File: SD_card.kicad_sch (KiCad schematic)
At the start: 1 part, among them J6 TF-15x15

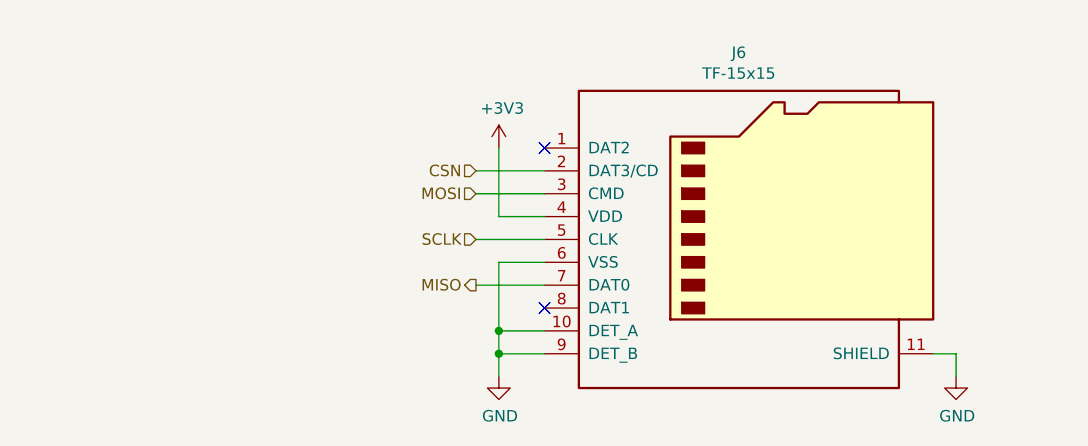
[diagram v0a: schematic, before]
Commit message: Move to KiCad v6, redesign circuit for chamber
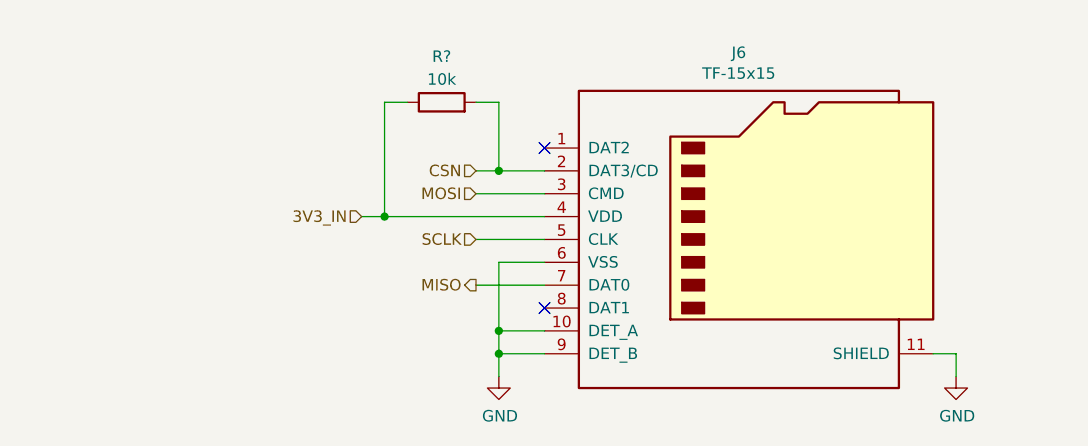
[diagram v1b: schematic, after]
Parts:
- added R?: 10k, Resistor_SMD:R_0603_1608Metric, symbol Device:R
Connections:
- net CSN: now also R?.2
- net +3V3 renamed 3V3_IN
- net 3V3_IN: now also R?.1
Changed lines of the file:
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@@
 (kicad_sch (version 20211123) (generator eeschema)
   (paper "A4")
+  (junction (at 127 91.44) (diameter 0) (color 0 0 0 0)
+  )
   (junction (at 127 109.22) (diameter 0) (color 0 0 0 0)
+  )
+  (junction (at 114.3 96.52) (diameter 0) (color 0 0 0 0)
   )
   (junction (at 127 111.76) (diameter 0) (color 0 0 0 0)
@@
   (no_connect (at 132.08 88.9))
   (no_connect (at 132.08 106.68))
+  (wire (pts (xy 114.3 96.52) (xy 132.08 96.52))
+    (stroke (width 0) (type default) (color 0 0 0 0))
+  )
+  (wire (pts (xy 127 91.44) (xy 132.08 91.44))
+    (stroke (width 0) (type default) (color 0 0 0 0))
+  )
+  (wire (pts (xy 116.84 83.82) (xy 114.3 83.82))
+    (stroke (width 0) (type default) (color 0 0 0 0))
+  )
+  (wire (pts (xy 111.76 96.52) (xy 114.3 96.52))
+    (stroke (width 0) (type default) (color 0 0 0 0))
+  )
   (wire (pts (xy 127 101.6) (xy 127 109.22))
     (stroke (width 0) (type default) (color 0 0 0 0))
   )
-  (wire (pts (xy 127 96.52) (xy 127 88.9))
+  (wire (pts (xy 127 83.82) (xy 127 91.44))
     (stroke (width 0) (type default) (color 0 0 0 0))
   )
@@
     (stroke (width 0) (type default) (color 0 0 0 0))
   )
-  (wire (pts (xy 132.08 96.52) (xy 127 96.52))
-    (stroke (width 0) (type default) (color 0 0 0 0))
-  )
   (wire (pts (xy 132.08 111.76) (xy 127 111.76))
     (stroke (width 0) (type default) (color 0 0 0 0))
   )
   (wire (pts (xy 124.46 99.06) (xy 132.08 99.06))
+    (stroke (width 0) (type default) (color 0 0 0 0))
+  )
+  (wire (pts (xy 114.3 83.82) (xy 114.3 96.52))
     (stroke (width 0) (type default) (color 0 0 0 0))
   )
@@
     (stroke (width 0) (type default) (color 0 0 0 0))
   )
-  (wire (pts (xy 124.46 91.44) (xy 132.08 91.44))
+  (wire (pts (xy 124.46 91.44) (xy 127 91.44))
     (stroke (width 0) (type default) (color 0 0 0 0))
   )
   (wire (pts (xy 127 111.76) (xy 127 114.3))
+    (stroke (width 0) (type default) (color 0 0 0 0))
+  )
+  (wire (pts (xy 127 83.82) (xy 124.46 83.82))
     (stroke (width 0) (type default) (color 0 0 0 0))
   )
@@
   )
   (hierarchical_label "MISO" (shape output) (at 124.46 104.14 180)
+    (effects (font (size 1.27 1.27)) (justify right))
+  )
+  (hierarchical_label "3V3_IN" (shape input) (at 111.76 96.52 180)
     (effects (font (size 1.27 1.27)) (justify right))
   )
@@
     )
     (property "Datasheet" "" (id 3) (at 127 114.3 0)
-      (effects (font (size 1.27 1.27)) hide)
-    )
-    (pin "1")
-  )
-  (symbol (lib_id "power:+3V3") (at 127 88.9 0) (unit 1)
-    (in_bom yes) (on_board yes)
-    (property "Reference" "#PWR013" (id 0) (at 127 92.71 0)
-      (effects (font (size 1.27 1.27)) hide)
-    )
-    (property "Value" "+3V3" (id 1) (at 127.381 84.5058 0))
-    (property "Footprint" "" (id 2) (at 127 88.9 0)
-      (effects (font (size 1.27 1.27)) hide)
-    )
-    (property "Datasheet" "" (id 3) (at 127 88.9 0)
       (effects (font (size 1.27 1.27)) hide)
     )
@@
     (pin "9")
   )
+  (symbol (lib_id "Device:R") (at 120.65 83.82 90) (unit 1)
+    (in_bom yes) (on_board yes)
+    (property "Reference" "R?" (id 0) (at 120.65 78.74 90))
+    (property "Value" "10k" (id 1) (at 120.65 81.28 90))
+    (property "Footprint" "Resistor_SMD:R_0603_1608Metric" (id 2) (at 120.65 85.598 90)
+      (effects (font (size 1.27 1.27)) hide)
+    )
+    (property "Datasheet" "~" (id 3) (at 120.65 83.82 0)
+      (effects (font (size 1.27 1.27)) hide)
+    )
+    (property "LCSC" "C25804" (id 4) (at 120.65 83.82 0)
+      (effects (font (size 1.27 1.27)) hide)
+    )
+    (pin "1")
+    (pin "2")
+  )
 )

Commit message: Add test points, add JLC part numbers to JST XH connectors, clean up
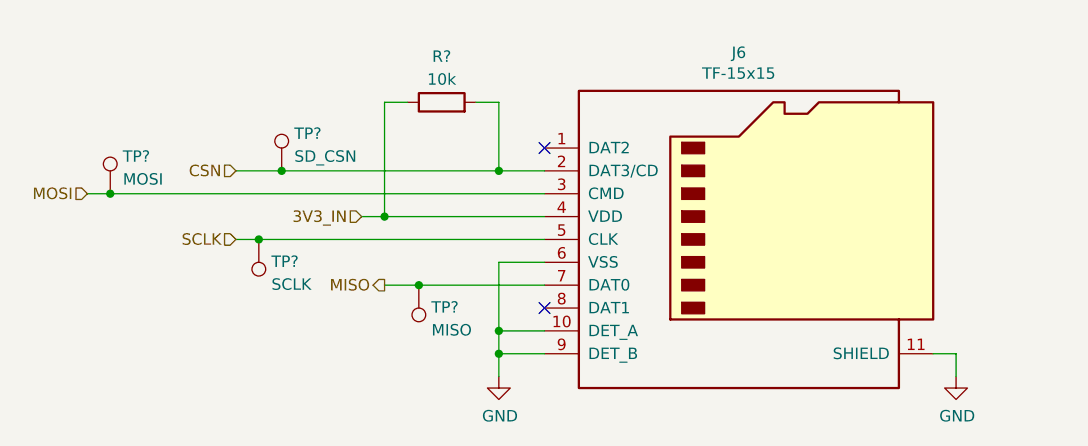
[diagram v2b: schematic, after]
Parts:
- added TP?: MOSI, symbol Connector:TestPoint
- added TP?: SD_CSN, symbol Connector:TestPoint
- added TP?: MISO, symbol Connector:TestPoint
- added TP?: SCLK, symbol Connector:TestPoint
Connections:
- net CSN: now also TP?.1
- net MISO: now also TP?.1
- net MOSI: now also TP?.1
- net SCLK: now also TP?.1
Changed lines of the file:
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@@
   (junction (at 127 109.22) (diameter 0) (color 0 0 0 0)
+  )
+  (junction (at 100.33 99.06) (diameter 0) (color 0 0 0 0)
+  )
+  (junction (at 118.11 104.14) (diameter 0) (color 0 0 0 0)
+  )
+  (junction (at 102.87 91.44) (diameter 0) (color 0 0 0 0)
+  )
+  (junction (at 83.82 93.98) (diameter 0) (color 0 0 0 0)
   )
   (junction (at 114.3 96.52) (diameter 0) (color 0 0 0 0)
@@
     (stroke (width 0) (type default) (color 0 0 0 0))
   )
+  (wire (pts (xy 100.33 99.06) (xy 132.08 99.06))
+    (stroke (width 0) (type default) (color 0 0 0 0))
+  )
   (wire (pts (xy 116.84 83.82) (xy 114.3 83.82))
     (stroke (width 0) (type default) (color 0 0 0 0))
@@
     (stroke (width 0) (type default) (color 0 0 0 0))
   )
-  (wire (pts (xy 124.46 104.14) (xy 132.08 104.14))
+  (wire (pts (xy 114.3 104.14) (xy 118.11 104.14))
     (stroke (width 0) (type default) (color 0 0 0 0))
   )
@@
     (stroke (width 0) (type default) (color 0 0 0 0))
   )
-  (wire (pts (xy 124.46 99.06) (xy 132.08 99.06))
+  (wire (pts (xy 97.79 99.06) (xy 100.33 99.06))
+    (stroke (width 0) (type default) (color 0 0 0 0))
+  )
+  (wire (pts (xy 118.11 104.14) (xy 132.08 104.14))
     (stroke (width 0) (type default) (color 0 0 0 0))
   )
@@
     (stroke (width 0) (type default) (color 0 0 0 0))
   )
+  (wire (pts (xy 83.82 93.98) (xy 132.08 93.98))
+    (stroke (width 0) (type default) (color 0 0 0 0))
+  )
   (wire (pts (xy 177.8 111.76) (xy 177.8 114.3))
     (stroke (width 0) (type default) (color 0 0 0 0))
   )
+  (wire (pts (xy 102.87 91.44) (xy 127 91.44))
+    (stroke (width 0) (type default) (color 0 0 0 0))
+  )
   (wire (pts (xy 175.26 111.76) (xy 177.8 111.76))
     (stroke (width 0) (type default) (color 0 0 0 0))
   )
-  (wire (pts (xy 124.46 93.98) (xy 132.08 93.98))
-    (stroke (width 0) (type default) (color 0 0 0 0))
-  )
-  (wire (pts (xy 124.46 91.44) (xy 127 91.44))
+  (wire (pts (xy 81.28 93.98) (xy 83.82 93.98))
+    (stroke (width 0) (type default) (color 0 0 0 0))
+  )
+  (wire (pts (xy 97.79 91.44) (xy 102.87 91.44))
     (stroke (width 0) (type default) (color 0 0 0 0))
   )
@@
     (stroke (width 0) (type default) (color 0 0 0 0))
   )
-  (hierarchical_label "SCLK" (shape input) (at 124.46 99.06 180)
-    (effects (font (size 1.27 1.27)) (justify right))
-  )
-  (hierarchical_label "MOSI" (shape input) (at 124.46 93.98 180)
-    (effects (font (size 1.27 1.27)) (justify right))
-  )
-  (hierarchical_label "MISO" (shape output) (at 124.46 104.14 180)
+  (hierarchical_label "SCLK" (shape input) (at 97.79 99.06 180)
+    (effects (font (size 1.27 1.27)) (justify right))
+  )
+  (hierarchical_label "MOSI" (shape input) (at 81.28 93.98 180)
+    (effects (font (size 1.27 1.27)) (justify right))
+  )
+  (hierarchical_label "MISO" (shape output) (at 114.3 104.14 180)
     (effects (font (size 1.27 1.27)) (justify right))
   )
@@
     (effects (font (size 1.27 1.27)) (justify right))
   )
-  (hierarchical_label "CSN" (shape input) (at 124.46 91.44 180)
+  (hierarchical_label "CSN" (shape input) (at 97.79 91.44 180)
     (effects (font (size 1.27 1.27)) (justify right))
   )
@@
     (pin "9")
   )
+  (symbol (lib_id "Connector:TestPoint") (at 83.82 93.98 0) (unit 1)
+    (in_bom yes) (on_board yes) (fields_autoplaced)
+    (property "Reference" "TP?" (id 0) (at 85.217 89.8433 0)
+      (effects (font (size 1.27 1.27)) (justify left))
+    )
+    (property "Value" "MOSI" (id 1) (at 85.217 92.3802 0)
+      (effects (font (size 1.27 1.27)) (justify left))
+    )
+    (property "Footprint" "" (id 2) (at 88.9 93.98 0)
+      (effects (font (size 1.27 1.27)) hide)
+    )
+    (property "Datasheet" "~" (id 3) (at 88.9 93.98 0)
+      (effects (font (size 1.27 1.27)) hide)
+    )
+    (pin "1")
+  )
   (symbol (lib_id "Device:R") (at 120.65 83.82 90) (unit 1)
     (in_bom yes) (on_board yes)
@@
     (pin "2")
   )
+  (symbol (lib_id "Connector:TestPoint") (at 102.87 91.44 0) (unit 1)
+    (in_bom yes) (on_board yes) (fields_autoplaced)
+    (property "Reference" "TP?" (id 0) (at 104.267 87.3033 0)
+      (effects (font (size 1.27 1.27)) (justify left))
+    )
+    (property "Value" "SD_CSN" (id 1) (at 104.267 89.8402 0)
+      (effects (font (size 1.27 1.27)) (justify left))
+    )
+    (property "Footprint" "" (id 2) (at 107.95 91.44 0)
+      (effects (font (size 1.27 1.27)) hide)
+    )
+    (property "Datasheet" "~" (id 3) (at 107.95 91.44 0)
+      (effects (font (size 1.27 1.27)) hide)
+    )
+    (pin "1")
+  )
+  (symbol (lib_id "Connector:TestPoint") (at 118.11 104.14 180) (unit 1)
+    (in_bom yes) (on_board yes) (fields_autoplaced)
+    (property "Reference" "TP?" (id 0) (at 119.507 106.6073 0)
+      (effects (font (size 1.27 1.27)) (justify right))
+    )
+    (property "Value" "MISO" (id 1) (at 119.507 109.1442 0)
+      (effects (font (size 1.27 1.27)) (justify right))
+    )
+    (property "Footprint" "" (id 2) (at 113.03 104.14 0)
+      (effects (font (size 1.27 1.27)) hide)
+    )
+    (property "Datasheet" "~" (id 3) (at 113.03 104.14 0)
+      (effects (font (size 1.27 1.27)) hide)
+    )
+    (pin "1")
+  )
+  (symbol (lib_id "Connector:TestPoint") (at 100.33 99.06 180) (unit 1)
+    (in_bom yes) (on_board yes) (fields_autoplaced)
+    (property "Reference" "TP?" (id 0) (at 101.727 101.5273 0)
+      (effects (font (size 1.27 1.27)) (justify right))
+    )
+    (property "Value" "SCLK" (id 1) (at 101.727 104.0642 0)
+      (effects (font (size 1.27 1.27)) (justify right))
+    )
+    (property "Footprint" "" (id 2) (at 95.25 99.06 0)
+      (effects (font (size 1.27 1.27)) hide)
+    )
+    (property "Datasheet" "~" (id 3) (at 95.25 99.06 0)
+      (effects (font (size 1.27 1.27)) hide)
+    )
+    (pin "1")
+  )
 )

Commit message: Add testpoint footprint assignments
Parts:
- TP18, TP19, TP20, TP21: renamed from TP?; footprint (none) -> TestPoint:TestPoint_Loop_D2.50mm_Drill1.0mm_LowProfile
- gave numbers to parts that had none: 1
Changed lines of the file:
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@@
   (symbol (lib_id "Connector:TestPoint") (at 83.82 93.98 0) (unit 1)
     (in_bom yes) (on_board yes) (fields_autoplaced)
-    (property "Reference" "TP?" (id 0) (at 85.217 89.8433 0)
+    (property "Reference" "TP18" (id 0) (at 85.217 89.8433 0)
       (effects (font (size 1.27 1.27)) (justify left))
     )
@@
       (effects (font (size 1.27 1.27)) (justify left))
     )
-    (property "Footprint" "" (id 2) (at 88.9 93.98 0)
+    (property "Footprint" "TestPoint:TestPoint_Loop_D2.50mm_Drill1.0mm_LowProfile" (id 2) (at 88.9 93.98 0)
       (effects (font (size 1.27 1.27)) hide)
     )
@@
   (symbol (lib_id "Device:R") (at 120.65 83.82 90) (unit 1)
     (in_bom yes) (on_board yes)
-    (property "Reference" "R?" (id 0) (at 120.65 78.74 90))
+    (property "Reference" "R9" (id 0) (at 120.65 78.74 90))
     (property "Value" "10k" (id 1) (at 120.65 81.28 90))
     (property "Footprint" "Resistor_SMD:R_0603_1608Metric" (id 2) (at 120.65 85.598 90)
@@
   (symbol (lib_id "Connector:TestPoint") (at 102.87 91.44 0) (unit 1)
     (in_bom yes) (on_board yes) (fields_autoplaced)
-    (property "Reference" "TP?" (id 0) (at 104.267 87.3033 0)
+    (property "Reference" "TP20" (id 0) (at 104.267 87.3033 0)
       (effects (font (size 1.27 1.27)) (justify left))
     )
@@
       (effects (font (size 1.27 1.27)) (justify left))
     )
-    (property "Footprint" "" (id 2) (at 107.95 91.44 0)
+    (property "Footprint" "TestPoint:TestPoint_Loop_D2.50mm_Drill1.0mm_LowProfile" (id 2) (at 107.95 91.44 0)
       (effects (font (size 1.27 1.27)) hide)
     )
@@
   (symbol (lib_id "Connector:TestPoint") (at 118.11 104.14 180) (unit 1)
     (in_bom yes) (on_board yes) (fields_autoplaced)
-    (property "Reference" "TP?" (id 0) (at 119.507 106.6073 0)
+    (property "Reference" "TP21" (id 0) (at 119.507 106.6073 0)
       (effects (font (size 1.27 1.27)) (justify right))
     )
@@
       (effects (font (size 1.27 1.27)) (justify right))
     )
-    (property "Footprint" "" (id 2) (at 113.03 104.14 0)
+    (property "Footprint" "TestPoint:TestPoint_Loop_D2.50mm_Drill1.0mm_LowProfile" (id 2) (at 113.03 104.14 0)
       (effects (font (size 1.27 1.27)) hide)
     )
@@
   (symbol (lib_id "Connector:TestPoint") (at 100.33 99.06 180) (unit 1)
     (in_bom yes) (on_board yes) (fields_autoplaced)
-    (property "Reference" "TP?" (id 0) (at 101.727 101.5273 0)
+    (property "Reference" "TP19" (id 0) (at 101.727 101.5273 0)
       (effects (font (size 1.27 1.27)) (justify right))
     )
@@
       (effects (font (size 1.27 1.27)) (justify right))
     )
-    (property "Footprint" "" (id 2) (at 95.25 99.06 0)
+    (property "Footprint" "TestPoint:TestPoint_Loop_D2.50mm_Drill1.0mm_LowProfile" (id 2) (at 95.25 99.06 0)
       (effects (font (size 1.27 1.27)) hide)
     )

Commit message: Finalize schematic
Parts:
- renumbered J6 to J13, R9 to R16, TP18 to TP20, TP19 to TP21, TP20 to TP22, TP21 to TP23
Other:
- title: (none) -> CO2 Chamber - SD Card
- moved on the sheet: J13, R16, TP20, TP21, TP22, TP23

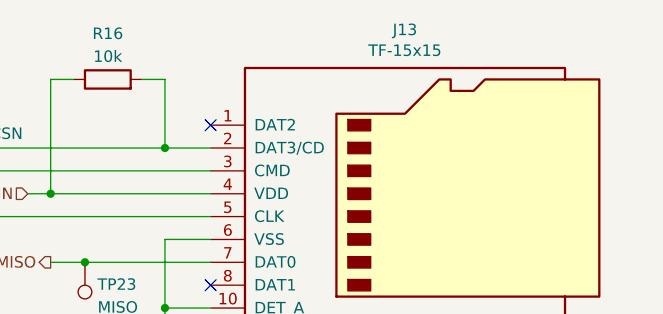
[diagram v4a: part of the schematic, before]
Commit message: Add voltage selection header for fan
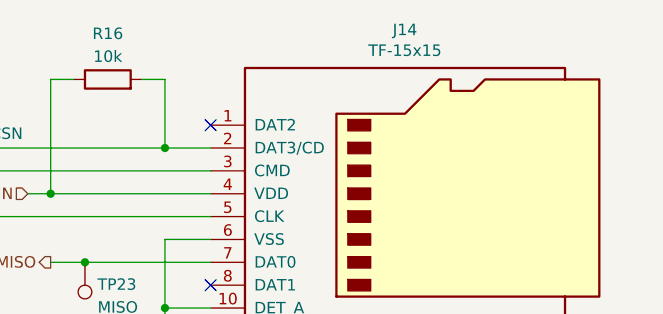
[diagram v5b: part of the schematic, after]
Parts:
- renumbered J13 to J14
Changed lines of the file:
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@@
   (symbol (lib_id "power:GND") (at 137.16 111.76 0) (unit 1)
     (in_bom yes) (on_board yes)
-    (property "Reference" "#PWR045" (id 0) (at 137.16 118.11 0)
+    (property "Reference" "#PWR046" (id 0) (at 137.16 118.11 0)
       (effects (font (size 1.27 1.27)) hide)
     )
@@
   (symbol (lib_id "power:GND") (at 187.96 111.76 0) (unit 1)
     (in_bom yes) (on_board yes)
-    (property "Reference" "#PWR046" (id 0) (at 187.96 118.11 0)
+    (property "Reference" "#PWR047" (id 0) (at 187.96 118.11 0)
       (effects (font (size 1.27 1.27)) hide)
     )
@@
   (symbol (lib_id "Connector:Micro_SD_Card_Det") (at 165.1 96.52 0) (unit 1)
     (in_bom yes) (on_board yes)
-    (property "Reference" "J13" (id 0) (at 163.83 75.7682 0))
+    (property "Reference" "J14" (id 0) (at 163.83 75.7682 0))
     (property "Value" "TF-15x15" (id 1) (at 163.83 78.0796 0))
     (property "Footprint" "co2_sensor_node:TF-15x15" (id 2) (at 217.17 78.74 0)

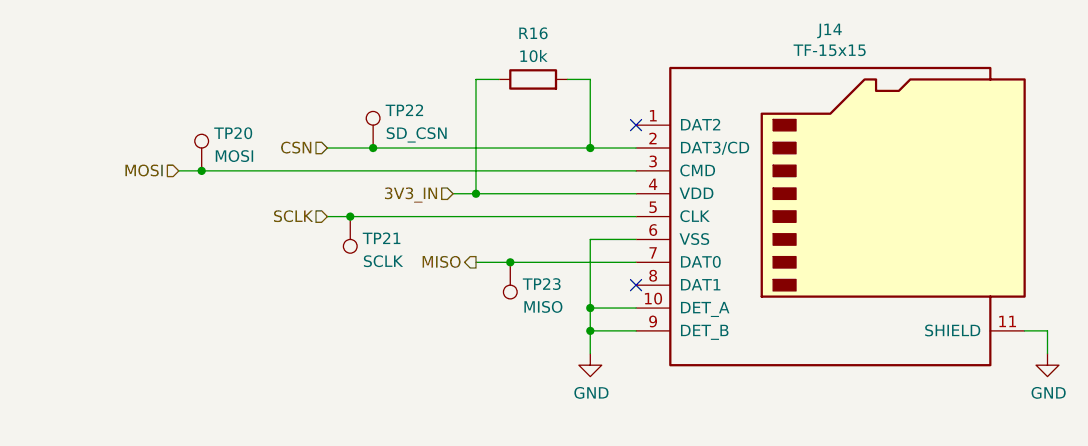
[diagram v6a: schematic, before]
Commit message: Finish rev. 2 schematic and begin PCB layout
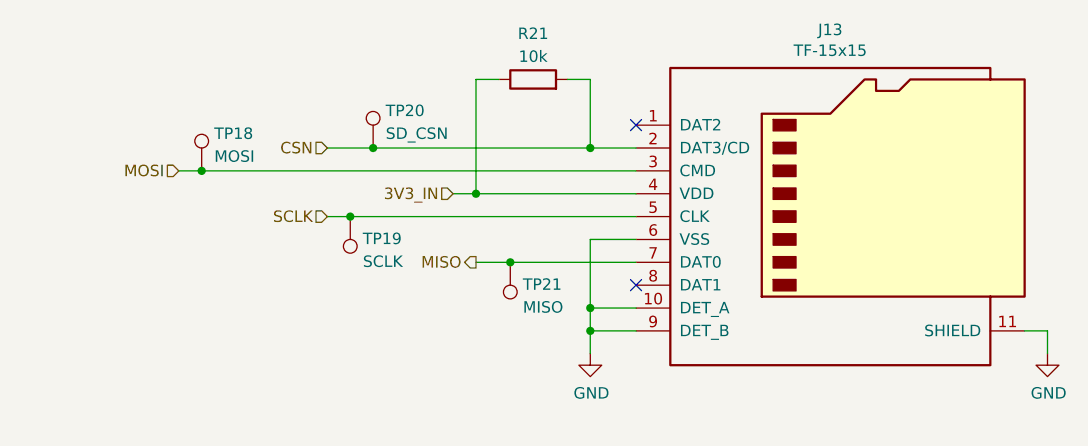
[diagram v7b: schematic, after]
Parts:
- renumbered J14 to J13, R16 to R21, TP20 to TP18, TP21 to TP19, TP22 to TP20, TP23 to TP21
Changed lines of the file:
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@@
   (symbol (lib_id "power:GND") (at 137.16 111.76 0) (unit 1)
     (in_bom yes) (on_board yes)
-    (property "Reference" "#PWR046" (id 0) (at 137.16 118.11 0)
+    (property "Reference" "#PWR052" (id 0) (at 137.16 118.11 0)
       (effects (font (size 1.27 1.27)) hide)
     )
@@
   (symbol (lib_id "power:GND") (at 187.96 111.76 0) (unit 1)
     (in_bom yes) (on_board yes)
-    (property "Reference" "#PWR047" (id 0) (at 187.96 118.11 0)
+    (property "Reference" "#PWR053" (id 0) (at 187.96 118.11 0)
       (effects (font (size 1.27 1.27)) hide)
     )
@@
   (symbol (lib_id "Connector:Micro_SD_Card_Det") (at 165.1 96.52 0) (unit 1)
     (in_bom yes) (on_board yes)
-    (property "Reference" "J14" (id 0) (at 163.83 75.7682 0))
+    (property "Reference" "J13" (id 0) (at 163.83 75.7682 0))
     (property "Value" "TF-15x15" (id 1) (at 163.83 78.0796 0))
     (property "Footprint" "co2_sensor_node:TF-15x15" (id 2) (at 217.17 78.74 0)
@@
   (symbol (lib_id "Connector:TestPoint") (at 93.98 91.44 0) (unit 1)
     (in_bom yes) (on_board yes) (fields_autoplaced)
-    (property "Reference" "TP20" (id 0) (at 95.377 87.3033 0)
+    (property "Reference" "TP18" (id 0) (at 95.377 87.3033 0)
       (effects (font (size 1.27 1.27)) (justify left))
     )
@@
   (symbol (lib_id "Device:R") (at 130.81 81.28 90) (unit 1)
     (in_bom yes) (on_board yes)
-    (property "Reference" "R16" (id 0) (at 130.81 76.2 90))
+    (property "Reference" "R21" (id 0) (at 130.81 76.2 90))
     (property "Value" "10k" (id 1) (at 130.81 78.74 90))
     (property "Footprint" "Resistor_SMD:R_0603_1608Metric" (id 2) (at 130.81 83.058 90)
@@
   (symbol (lib_id "Connector:TestPoint") (at 113.03 88.9 0) (unit 1)
     (in_bom yes) (on_board yes) (fields_autoplaced)
-    (property "Reference" "TP22" (id 0) (at 114.427 84.7633 0)
+    (property "Reference" "TP20" (id 0) (at 114.427 84.7633 0)
       (effects (font (size 1.27 1.27)) (justify left))
     )
@@
   (symbol (lib_id "Connector:TestPoint") (at 128.27 101.6 180) (unit 1)
     (in_bom yes) (on_board yes) (fields_autoplaced)
-    (property "Reference" "TP23" (id 0) (at 129.667 104.0673 0)
+    (property "Reference" "TP21" (id 0) (at 129.667 104.0673 0)
       (effects (font (size 1.27 1.27)) (justify right))
     )
@@
   (symbol (lib_id "Connector:TestPoint") (at 110.49 96.52 180) (unit 1)
     (in_bom yes) (on_board yes) (fields_autoplaced)
-    (property "Reference" "TP21" (id 0) (at 111.887 98.9873 0)
+    (property "Reference" "TP19" (id 0) (at 111.887 98.9873 0)
       (effects (font (size 1.27 1.27)) (justify right))
     )
